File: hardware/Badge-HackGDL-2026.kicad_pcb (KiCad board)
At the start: 2 copper layers, 150 x 100 mm, 135 parts, among them J1 Conn_01x20, J10 Battery, J2 Conn_01x04_Pin, J4 Conn_01x08, J5 Conn_01x08, J6 Conn_01x08, J7 Conn_01x08, J9 Add_On, P4 USB_C_Plug_USB2.0, Q1 DMG3415U-7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

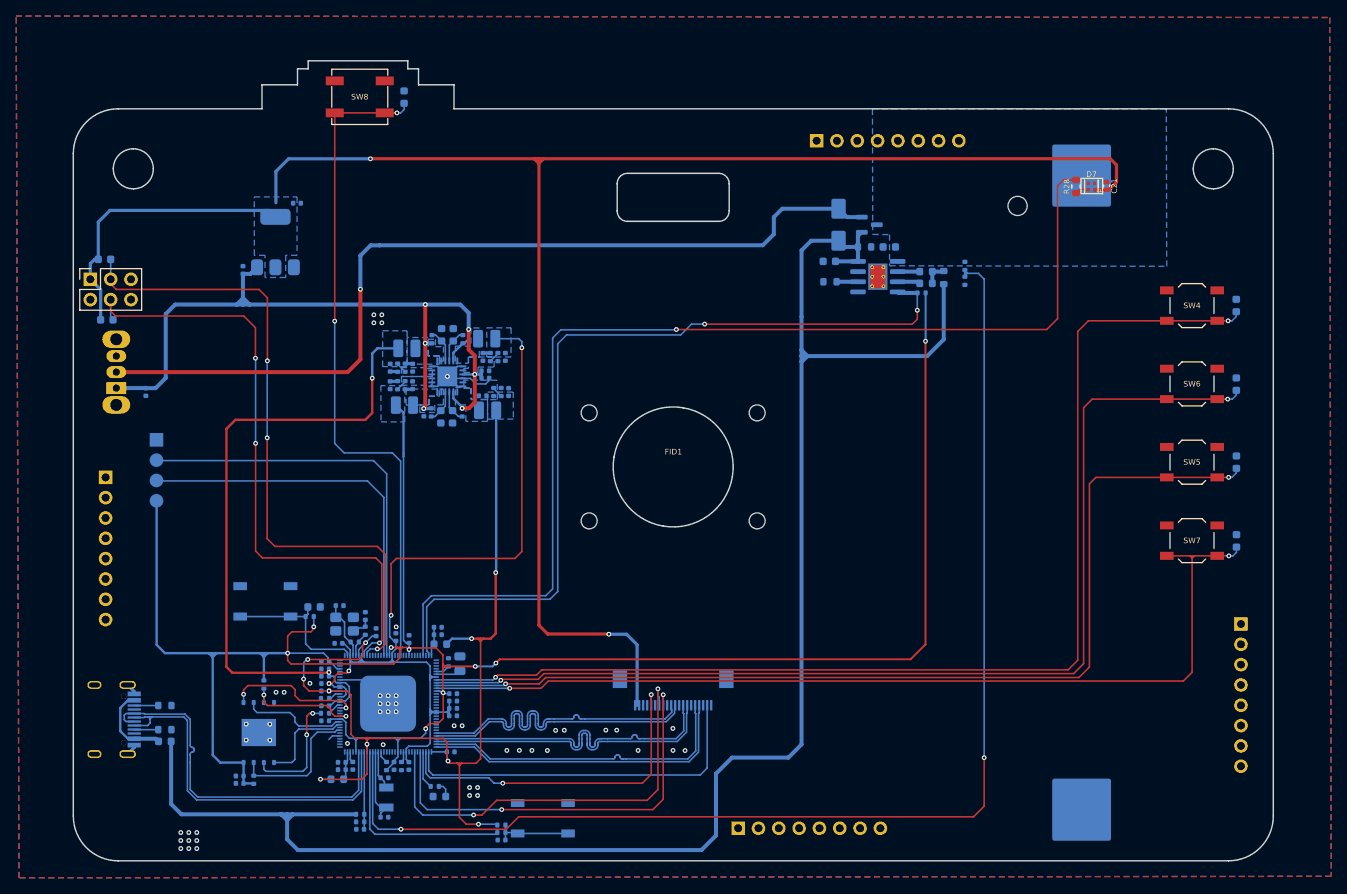
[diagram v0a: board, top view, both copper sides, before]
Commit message: feat(Hw):Update_Labels
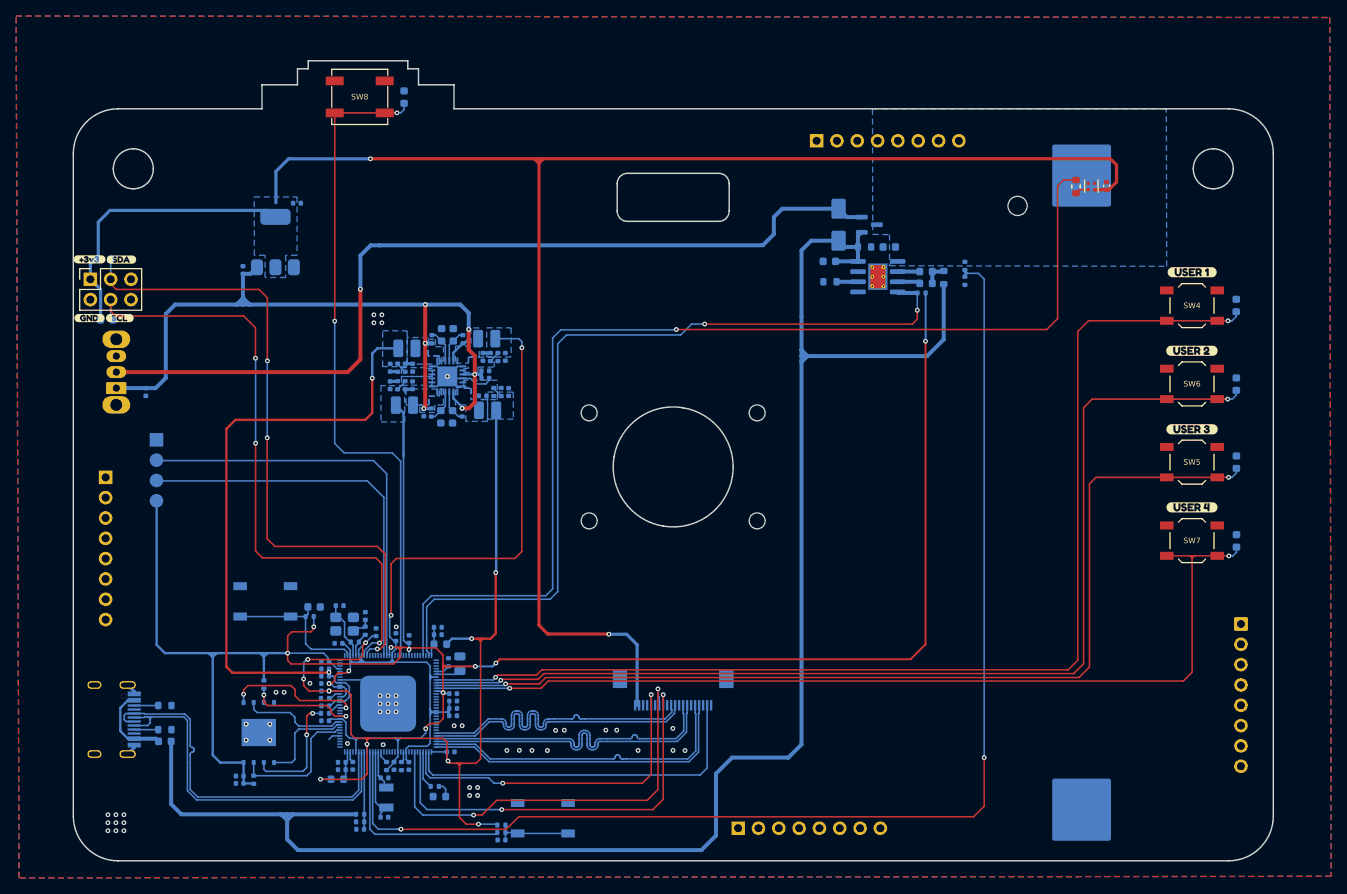
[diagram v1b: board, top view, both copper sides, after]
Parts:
- added kibuzzard-684B03BD: G***, kibuzzard-684B03BD, B.Cu at (81.8, 71.7)
- added kibuzzard-684B03C9: G***, kibuzzard-684B03C9, B.Cu at (82.1, 68.3)
- added kibuzzard-684B03D5: G***, kibuzzard-684B03D5, B.Cu at (95.4, 95.9)
- added kibuzzard-6892465C: G***, kibuzzard-6892465C, B.Cu at (130.1, 123.0)
- added kibuzzard-69714845: G***, kibuzzard-69714845, F.Cu at (73.5, 57.1)
- added kibuzzard-69714866: G***, kibuzzard-69714866, F.Cu at (73.5, 64.4)
- added kibuzzard-6971487E: G***, kibuzzard-6971487E, F.Cu at (77.5, 57.1)
- added kibuzzard-6971488E: G***, kibuzzard-6971488E, F.Cu at (77.2, 64.4)
- added kibuzzard-69714B9C: G***, kibuzzard-69714B9C, B.Cu at (86.2, 87.3)
- added kibuzzard-69714BBC: G***, kibuzzard-69714BBC, B.Cu at (85.6, 84.8)
- added kibuzzard-69714BDE: G***, kibuzzard-69714BDE, B.Cu at (85.5, 82.2)
- added kibuzzard-69714C02: G***, kibuzzard-69714C02, B.Cu at (86.0, 79.6)
- added kibuzzard-69714C5E: G***, kibuzzard-69714C5E, F.Cu at (211.3, 58.7)
- added kibuzzard-69714C72: G***, kibuzzard-69714C72, F.Cu at (211.3, 68.5)
- added kibuzzard-69714C98: G***, kibuzzard-69714C98, F.Cu at (211.3, 78.3)
- added kibuzzard-69714CA0: G***, kibuzzard-69714CA0, F.Cu at (211.3, 88.1)
